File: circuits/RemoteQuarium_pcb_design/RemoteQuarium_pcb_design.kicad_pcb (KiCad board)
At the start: 2 copper layers, 32 parts, among them J1 Power_terminal, J10 LCD_pins, J11 Feeder_servo_pins, J12 ESP_pins, J13 PH_sensor_sockets, J14 Ph_sesnor-pins, J15 Power & D3-D4, J2 ESP left side sockets, J3 ESP right side sockets, J4 Relay_terminal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

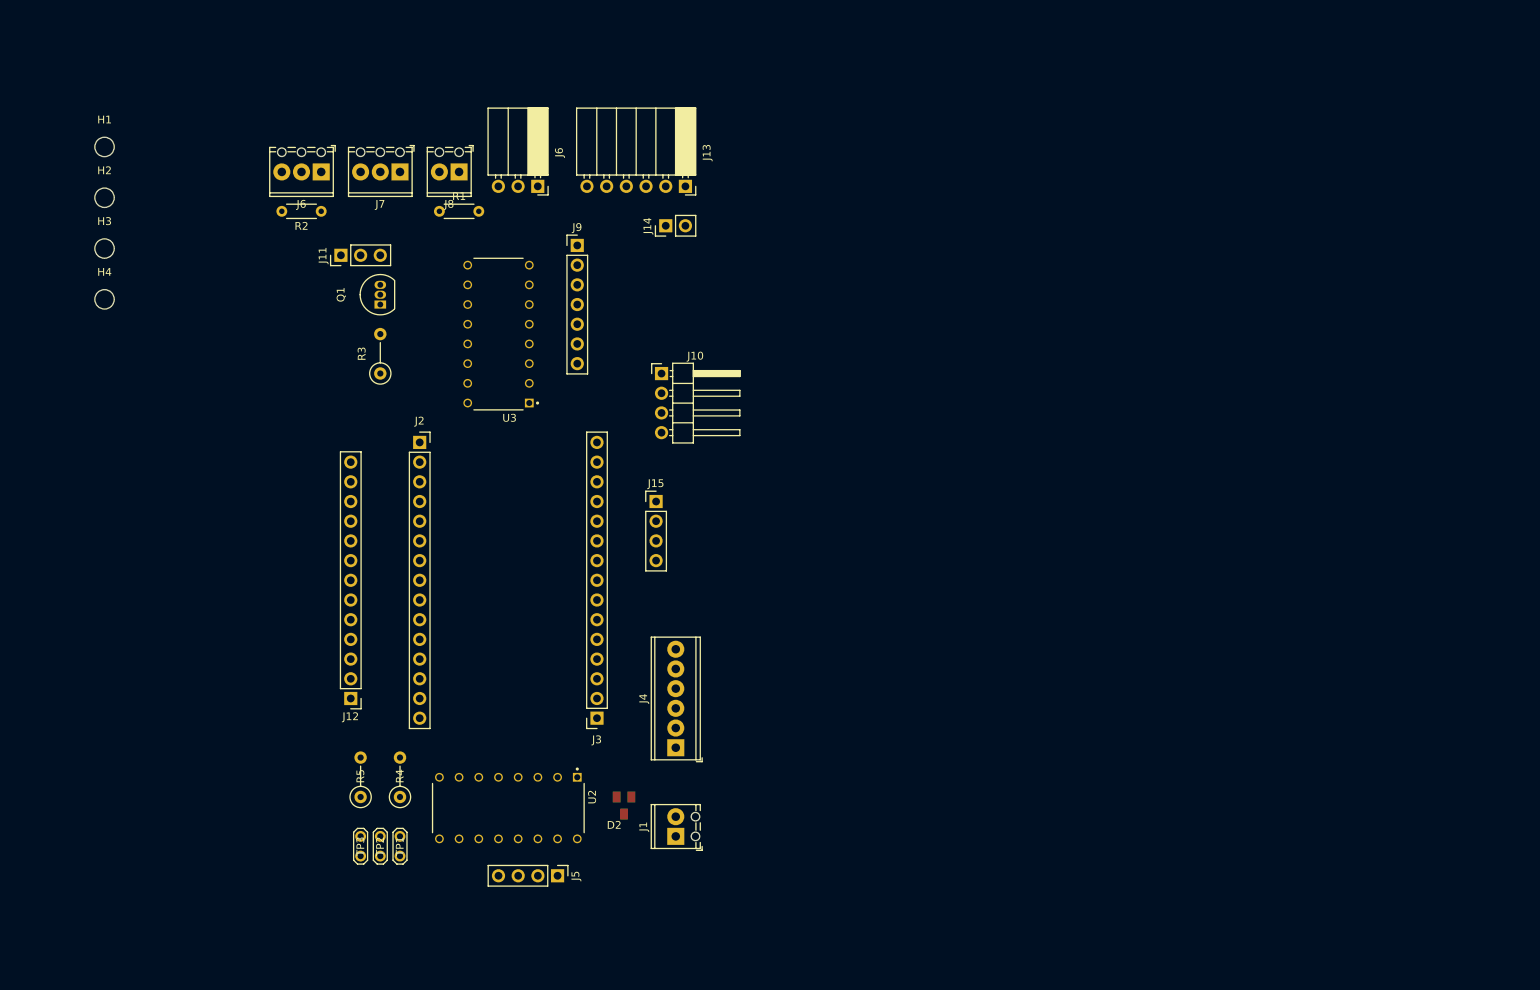
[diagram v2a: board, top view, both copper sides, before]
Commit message: Fixed ESP memory leak xd. Fixed wrong samplePeriod enum numbering. Fixed up relay switching. Also added WDT and runtime measuring. Fixed up wrong time formatting in app. Fixed a lot of stuff actually xdd
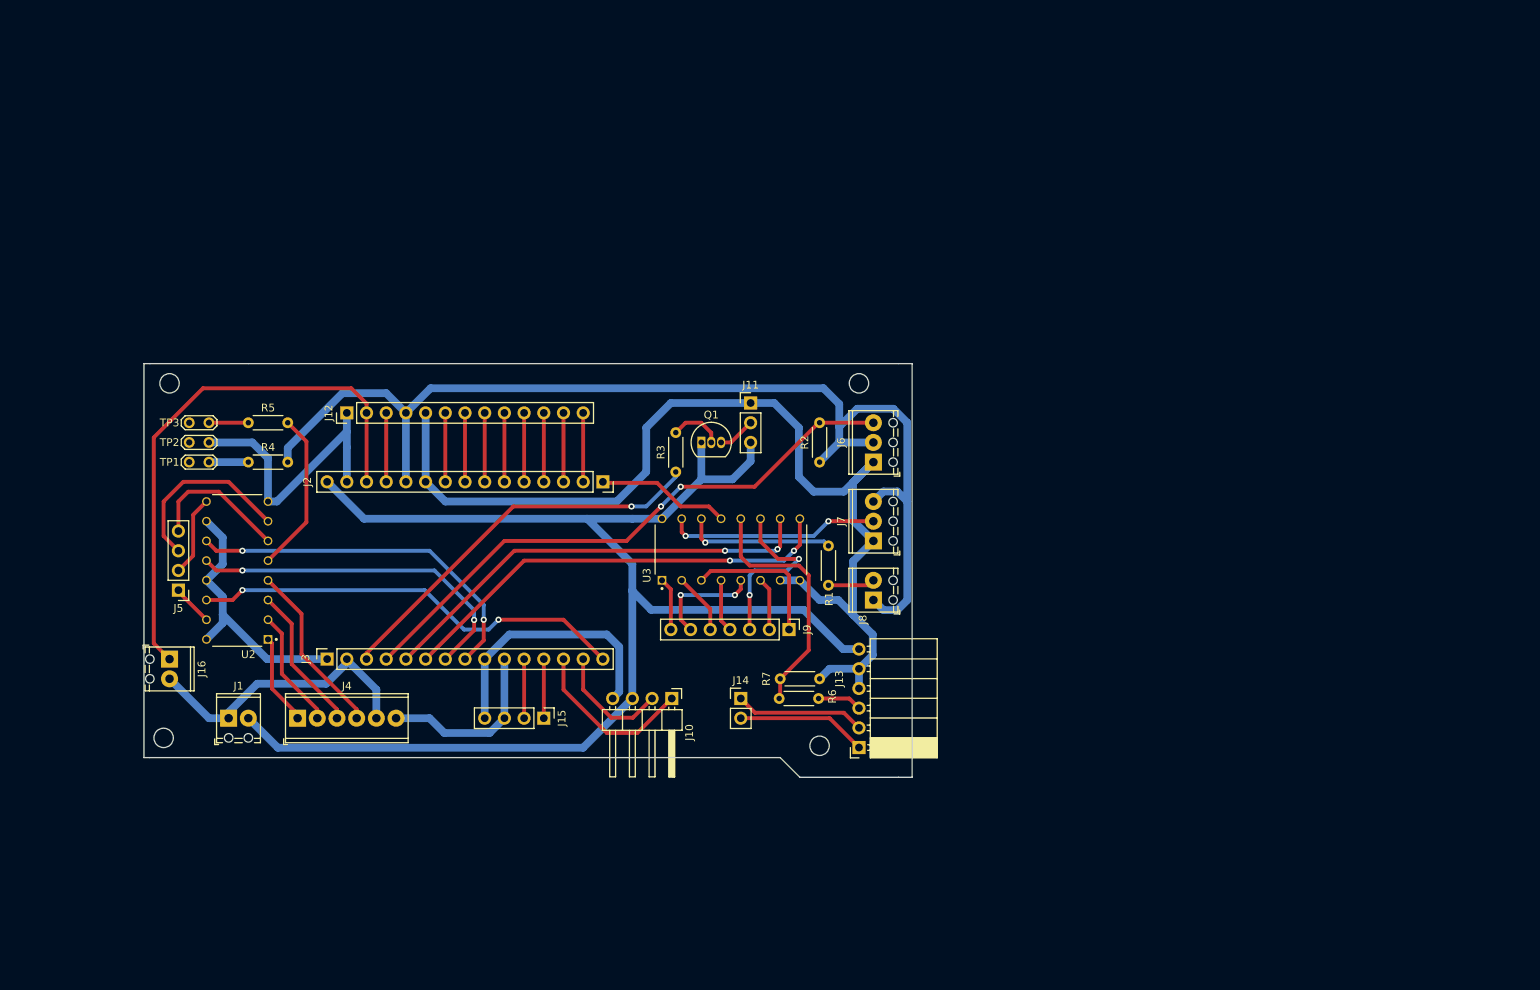
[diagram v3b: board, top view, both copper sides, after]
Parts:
- removed D2: PESD5V0S2BT, PESD5V0S2BT:SOT23
- removed the J6 at (144.8, 50.8)
- added J16: Reset_button_terminal, TerminalBlock_Phoenix:TerminalBlock_Phoenix_MPT-0,5-2-2.54_1x02_P2.54mm_Horizontal, F.Cu at (97.3, 111.8)
- added R6: 1KR, Resistor_THT:R_Axial_DIN0204_L3.6mm_D1.6mm_P5.08mm_Horizontal, F.Cu at (175.9, 116.8)
- added R7: 2KR, Resistor_THT:R_Axial_DIN0204_L3.6mm_D1.6mm_P5.08mm_Horizontal, F.Cu at (181.1, 114.3)
- R3, R4, R5: footprint Resistor_THT:R_Axial_DIN0207_L6.3mm_D2.5mm_P5.08mm_Vertical -> Resistor_THT:R_Axial_DIN0204_L3.6mm_D1.6mm_P5.08mm_Horizontal
- moved H2 116.2 mm to (181.1, 122.9), turned to -90 degrees
- moved H1 101.9 mm to (186.2, 76.2), turned to -90 degrees
- moved J6 80.4 mm to (188.0, 86.4), turned to 90 degrees
- moved J7 77.4 mm to (188.0, 96.5), turned to 90 degrees
- moved J8 76.8 mm to (188.0, 104.1), turned to 90 degrees
- moved J13 75.7 mm to (186.2, 123.2), turned to 180 degrees
- moved R2 71.9 mm to (181.1, 86.4), turned to 90 degrees
- moved R1 69.6 mm to (182.2, 102.2), turned to 90 degrees
- moved J14 61.7 mm to (170.9, 116.8), turned to 0 degrees
- moved J5 61.2 mm to (98.4, 102.9), turned to 180 degrees
- moved J1 59.6 mm to (104.9, 119.4), turned to 0 degrees
- moved H4 57.1 mm to (96.5, 121.9)
- moved TP3 56.8 mm to (102.4, 81.3), turned to 180 degrees
- moved J9 56.6 mm to (177.2, 108.0), turned to -90 degrees
- moved J11 56.2 mm to (172.2, 78.7), turned to 0 degrees
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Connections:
- net /GH renamed /QH
- net Net-(Q1-B) renamed /TXR
- net Net-(R4-Pad1) renamed /VCCR
- net Net-(R5-Pad1) renamed /R_LEDR
- J11 pad 2: /TX -> /TX5V
- J5 pad 2: /QG -> /QH'
- J5 pad 4: /GH' -> /QG
- Q1 pad 3: /TX -> /TX5V
- R1 pad 2: /LIGHT_DAT -> /LIGHT_DATR
- U2 pad 9: /GH' -> /QH'
- U3 pad 12: /P0 -> /P0R
- U3 pad 14: /LIGHT_DAT -> /LIGHT_DATR
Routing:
- net /GND: track 0.00 -> 246.3 mm
- net /VCC: track 0.00 -> 202.9 mm
- net /VIN: track 0.00 -> 178.6 mm
- net /RX: track 0.00 -> 75.4 mm, vias 0 -> 2
- net /RST: track 0.00 -> 70.4 mm
- net /D8: track 0.00 -> 57.9 mm, vias 0 -> 2
- net /D7: track 0.00 -> 57.7 mm, vias 0 -> 2
- net /D0: track 0.00 -> 56.4 mm, vias 0 -> 2
- net /TX: track 0.00 -> 50.7 mm, vias 0 -> 1
- net /D5: track 0.00 -> 47.2 mm, vias 0 -> 2
- net /D6: track 0.00 -> 45.0 mm, vias 0 -> 2
- net /P0R: track 0.00 -> 32.1 mm
- net /WATER_DAT: track 0.00 -> 27.4 mm, vias 0 -> 2
- net /QH: track 0.00 -> 23.8 mm
- net /X3: track 0.00 -> 23.0 mm, vias 0 -> 2
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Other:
- board outline added: 99.1 x 53.3 mm

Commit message: Added more complex logging and notification testing should work, app builds and is usable, but need to add react SVG libs for the charts to workgit add .
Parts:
- added Q2: BC547, Package_TO_SOT_THT:TO-92_Inline, F.Cu at (128.9, 116.2)
- added Q3: BC547, Package_TO_SOT_THT:TO-92_Inline, F.Cu at (123.1, 116.2)
- added Q4: BC547, Package_TO_SOT_THT:TO-92_Inline, F.Cu at (117.3, 116.2)
- added Q5: BC547, Package_TO_SOT_THT:TO-92_Inline, F.Cu at (111.5, 116.2)
- moved J4 6.66 mm to (118.7, 123.8)
- moved J1 4.06 mm to (103.5, 123.2)
- moved J15 2.60 mm to (147.3, 121.3)
- moved H4 2.54 mm to (96.5, 124.5)
- moved H2 2.22 mm to (181.6, 125.1)
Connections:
- J4 pad 1: /S0 -> /S05V
- J4 pad 2: /S1 -> /S15V
- J4 pad 3: /S2 -> /S25V
- J4 pad 4: /S3 -> /S35V
- J4 pad 6: /VCC -> /VIN
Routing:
- net /GND: track 246.3 -> 284.9 mm, vias 0 -> 1
- net /VIN: track 178.6 -> 209.5 mm
- net /VCC: track 202.9 -> 189.2 mm
- net /S05V: track 0.00 -> 10.4 mm
- net /S15V: track 0.00 -> 7.14 mm
- net /S3: track 22.5 -> 28.9 mm
- net /S35V: track 0.00 -> 6.13 mm
- net /S25V: track 0.00 -> 5.37 mm
- net /S2: track 18.9 -> 21.7 mm
- net /D4: track 7.62 -> 10.3 mm
- net /D3: track 7.62 -> 10.3 mm
- net /S0: track 11.7 -> 9.43 mm
- net /S1: track 15.3 -> 14.4 mm
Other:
- outline, holes or cut-outs redrawn
- board text added: "5V!"
- board text added: "D"
- board text added: "D0"
- board text added: "D3"
- board text added: "D4"
- board text added: "DAT"
- board text added: "ESP port and sensor interface board for ATC system v1.0 Power terminal takes 5V = VIN ESP power is 5V and VCC = 3.3V Designed by Abel Takacs"
- board text added: "G"
- board text added: "GND"
- board text added: "LCD I2C"
- board text added: "LIGHT"
- board text added: "Ph module"
- board text added: "S2 S1 S0"
- board text added: "S3 GND 5V"
- board text added: "SCL"
- board text added: "SDA"
- board text added: "SERVO"
- board text added: "T0"
- board text added: "TEMP"
- board text added: "V+"
- board text added: "VCC"
- board text added: "VIN"
- board text added: "WATER"

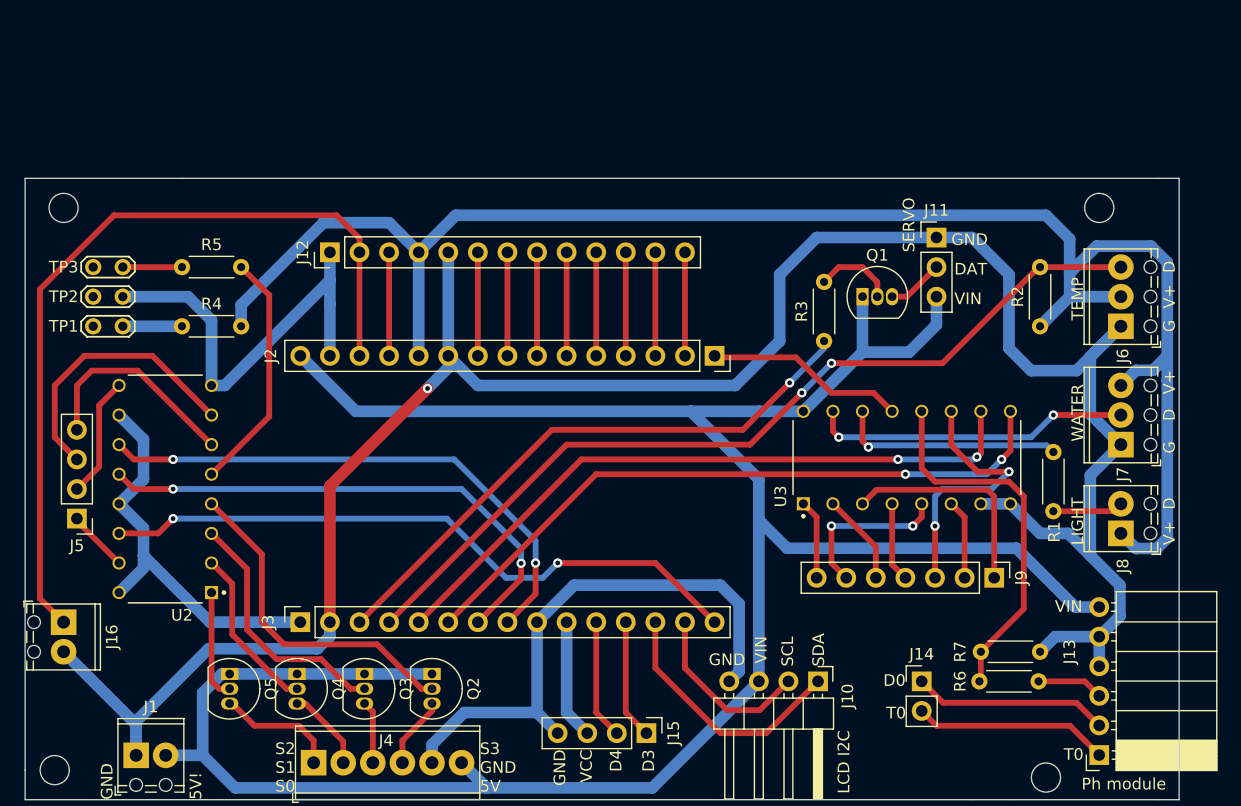
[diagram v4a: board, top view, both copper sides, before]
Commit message: Minor changes to the strings and to notification are working, also made a working dev build
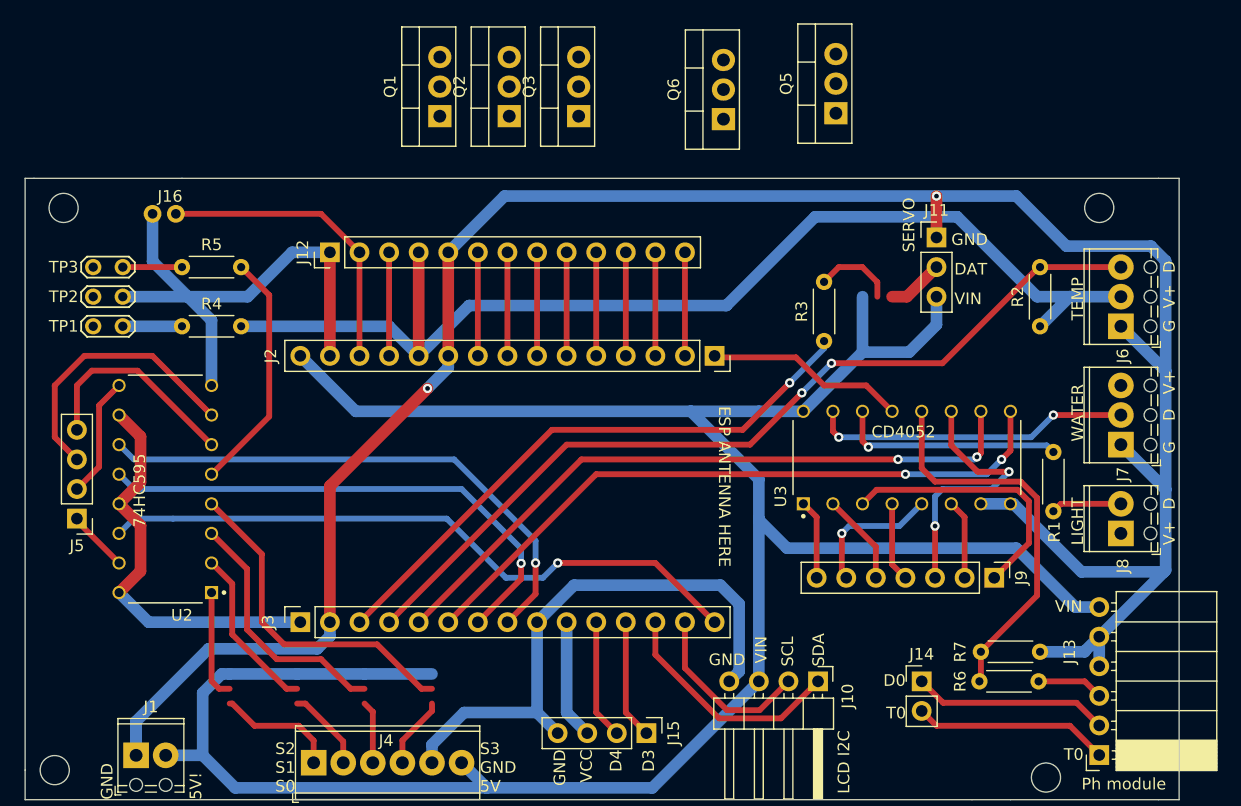
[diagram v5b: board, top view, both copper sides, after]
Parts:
- removed Q4: BC547, Package_TO_SOT_THT:TO-92_Inline
- added Q6: IRLZ34N, Package_TO_SOT_THT:TO-220-3_Vertical, F.Cu at (153.9, 68.6)
- J16: footprint TerminalBlock_Phoenix:TerminalBlock_Phoenix_MPT-0,5-2-2.54_1x02_P2.54mm_Horizontal -> NXW:NXW-02P
- Q1, Q2, Q3, Q5: value BC547 -> IRLZ34N; footprint Package_TO_SOT_THT:TO-92_Inline -> Package_TO_SOT_THT:TO-220-3_Vertical
- moved Q5 70.9 mm to (163.6, 68.1), turned to 90 degrees
- moved Q3 51.3 mm to (141.5, 68.3), turned to 90 degrees
- moved Q2 48.3 mm to (135.5, 68.3), turned to 90 degrees
- moved Q1 39.5 mm to (129.6, 68.3), turned to 90 degrees
- moved J16 35.9 mm to (104.9, 76.7), turned to 0 degrees
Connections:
- Q1 pad 1: /VIN -> /S1
- Q1 pad 2: /TXR -> /S15V
- Q1 pad 3: /TX5V -> /VIN
- Q2 pad 1: /VIN -> /S2
- Q2 pad 2: /S3 -> /S25V
- Q2 pad 3: /S35V -> /VIN
- Q3 pad 1: /VIN -> /S3
- Q3 pad 2: /S2 -> /S35V
- Q3 pad 3: /S25V -> /VIN
- Q5 pad 1: /VIN -> /TXR
- Q5 pad 2: /S0 -> /VIN
- Q5 pad 3: /S05V -> /TX5V
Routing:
- net /VCC: track 189.2 -> 142.0 mm
- net /RST: track 70.4 -> 26.0 mm
- net /GND: track 284.9 -> 297.4 mm, vias 1 -> 2
- net /Y: track 19.0 -> 23.0 mm
- net /Y1: track 14.2 -> 11.9 mm, vias 2 -> 1
- net /SDA: track 22.1 -> 20.3 mm
- net /P0R: track 32.1 -> 33.6 mm
- net /D6: vias 2 -> 1
- net /D5: vias 2 -> 1
- net /D0: vias 2 -> 1
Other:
- board text added: "74HC595"
- board text added: "CD4052"
- board text added: "ESP ANTENNA HERE"
- board text added: "ESP port and sensor interface board for ATC system v1.0"
- board text removed: "ESP port and sensor interface board for ATC system v1.0 Power terminal takes 5V = VIN ESP power is 5V and VCC = 3.3V Designed by Abel Takacs"
